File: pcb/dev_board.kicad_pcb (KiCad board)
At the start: 6 copper layers, 45.7 x 41.2 mm, 39 parts, among them J1 Conn_02x13_Odd_Even, J2 Conn_02x13_Odd_Even, J4 Conn_01x05, SW1 SW_DIP_x03, SW2 Start, U1 XS-LPC-01, U2 MCP3202, U3 NCP114ASN280T1G, U6 TLV74311

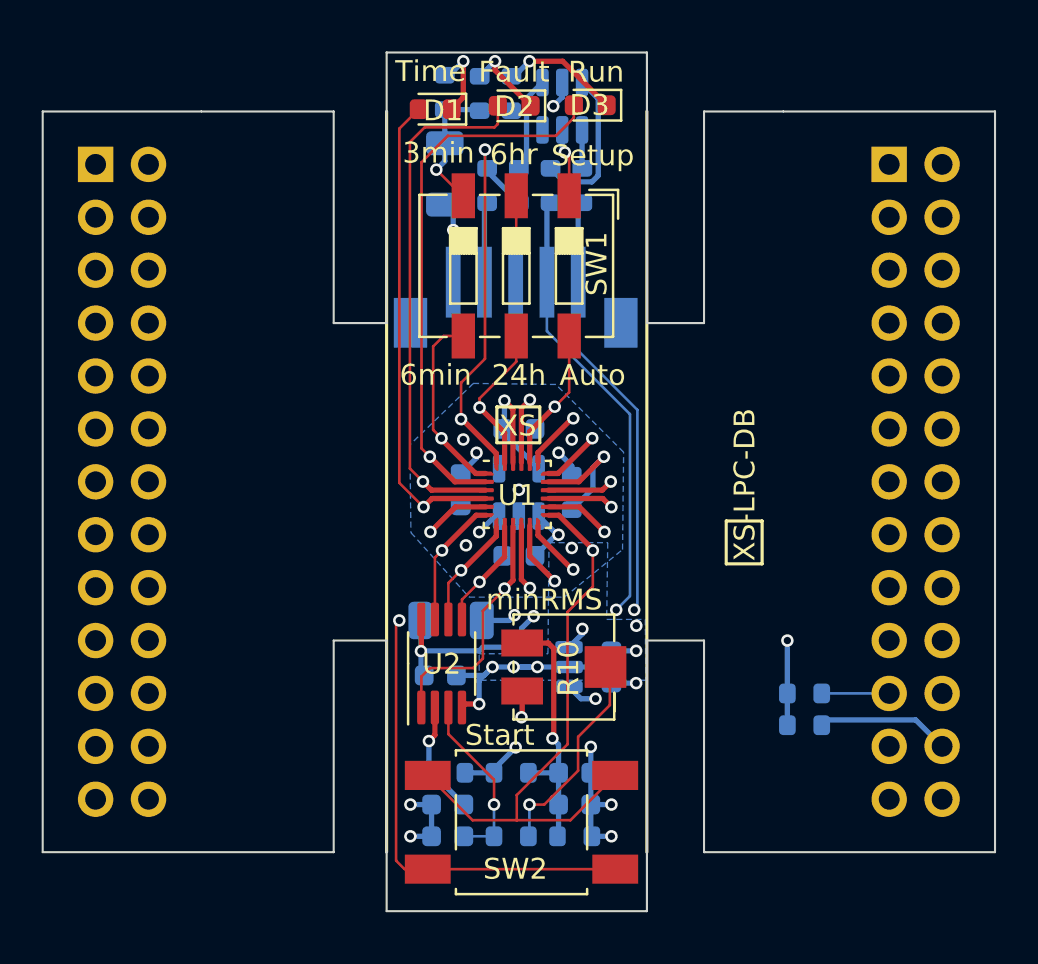
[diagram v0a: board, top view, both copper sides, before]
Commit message: PCB Tapeout v0.5 LPC_DB development board, schematic, bom, datasheets updated.
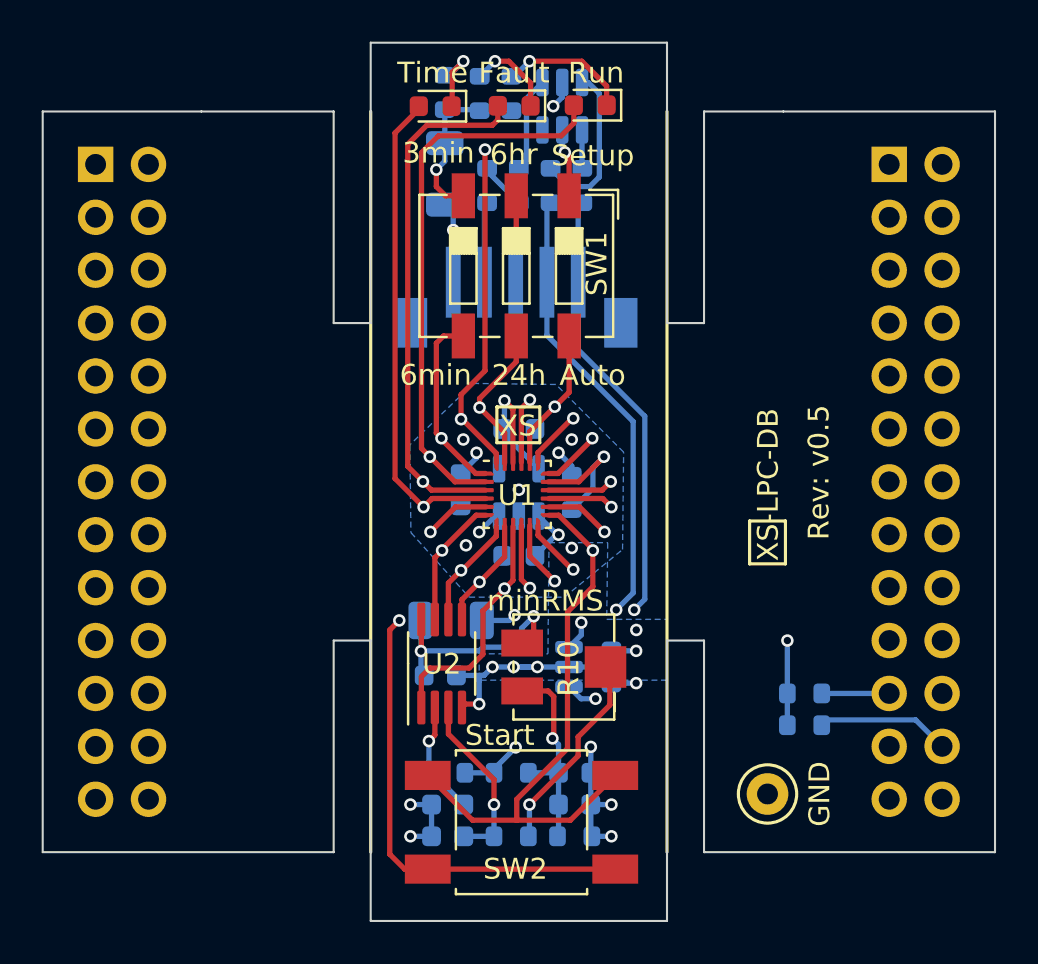
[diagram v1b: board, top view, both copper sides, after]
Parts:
- added TP1: GND, TestPoint:TestPoint_Keystone_5000-5004_Miniature, F.Cu at (182.1, 119.1)
- moved D1 0.14 mm to (166.2, 86.1)
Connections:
- R10 pad 1: +3V0 -> /CT2
- R10 pad 3: /CT2 -> +3V0
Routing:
- net /CT2: track 40.6 -> 38.6 mm
- net Net-(D3-K): track 5.61 -> 6.14 mm
- net GND: track 68.6 -> 69.1 mm
- net +3V0: track 11.8 -> 12.0 mm, vias 3 -> 2
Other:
- board size 45.7 x 41.2 mm -> 45.7 x 42.2 mm
- board text added: "(c) Eric Pearson 2026"
- board text added: "Rev: ${REVISION}"
